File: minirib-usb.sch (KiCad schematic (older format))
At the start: 21 parts

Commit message: added test connector
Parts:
- added J?: Test_header, symbol Connector:Conn_01x06_Male
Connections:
- wire segments 65 -> 67
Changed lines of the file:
@@
 Wire Wire Line
 	5900 4750 5800 4750
+$Comp
+L Connector:Conn_01x06_Male J?
+U 1 1 610DD5AA
+P 8000 3000
+F 0 "J?" H 8200 3450 50  0000 C CNN
+F 1 "Test_header" H 8200 3350 50  0000 C CNN
+F 2 "" H 8000 3000 50  0001 C CNN
+F 3 "~" H 8000 3000 50  0001 C CNN
+	1    8000 3000
+	1    0    0    -1
+$EndComp
+$Comp
+L power:GND #PWR?
+U 1 1 610E094D
+P 8600 2850
+F 0 "#PWR?" H 8600 2600 50  0001 C CNN
+F 1 "GND" H 8605 2677 50  0001 C CNN
+F 2 "" H 8600 2850 50  0001 C CNN
+F 3 "" H 8600 2850 50  0001 C CNN
+	1    8600 2850
+	1    0    0    -1
+$EndComp
+Wire Wire Line
+	8200 2800 8600 2800
+Wire Wire Line
+	8600 2800 8600 2850
+Text GLabel 8200 2900 2    50   Input ~ 0
+~BUSY
+Text GLabel 8200 3000 2    50   Input ~ 0
+BUSY
+Text GLabel 8200 3100 2    50   Input ~ 0
+BUS-
+Text GLabel 8200 3200 2    50   Input ~ 0
+BUS+
+Text GLabel 8200 3300 2    50   Input ~ 0
+BIAS
 $EndSCHEMATC

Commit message: schematic rework
more closely following the original RIB schematic
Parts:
- removed Q?: 2N3906, symbol Device:Q_PNP_BCE
- removed Q? (x2): 2N3904, symbol Device:Q_NPN_BCE
- removed R? (x5): 4k7, symbol Device:R_Small
- removed U?: CA3140, symbol Amplifier_Operational:CA3140
- added C? (x5): 220pF, symbol Device:C_Small
- added D? (x4): D_TVS, symbol Device:D_TVS
- added D?: TXLED, symbol Device:LED_Small
- added D?: RXLED, symbol Device:LED_Small
- added Q? (x2): 2N3906, Package_TO_SOT_THT:TO-92_Inline, symbol Transistor_BJT:2N3906
- added Q? (x5): 2N3904, Package_TO_SOT_THT:TO-92_Inline, symbol Transistor_BJT:2N3904
- added R? (x8): 4k7, symbol Device:R_Small
- added R? (x2): 2k2, symbol Device:R_Small
- added R?: 20k, symbol Device:R_Small
- added R?: 3k, symbol Device:R_Small
- added R? (x3): 1k5, symbol Device:R_Small
- added U?: LM311, symbol Comparator:LM311
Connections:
- net labels added: ~CTS, ~DTR
- wire segments 67 -> 118
- no-connect marks 7 -> 8
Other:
- moved on the sheet: C?, J?, R?, U?

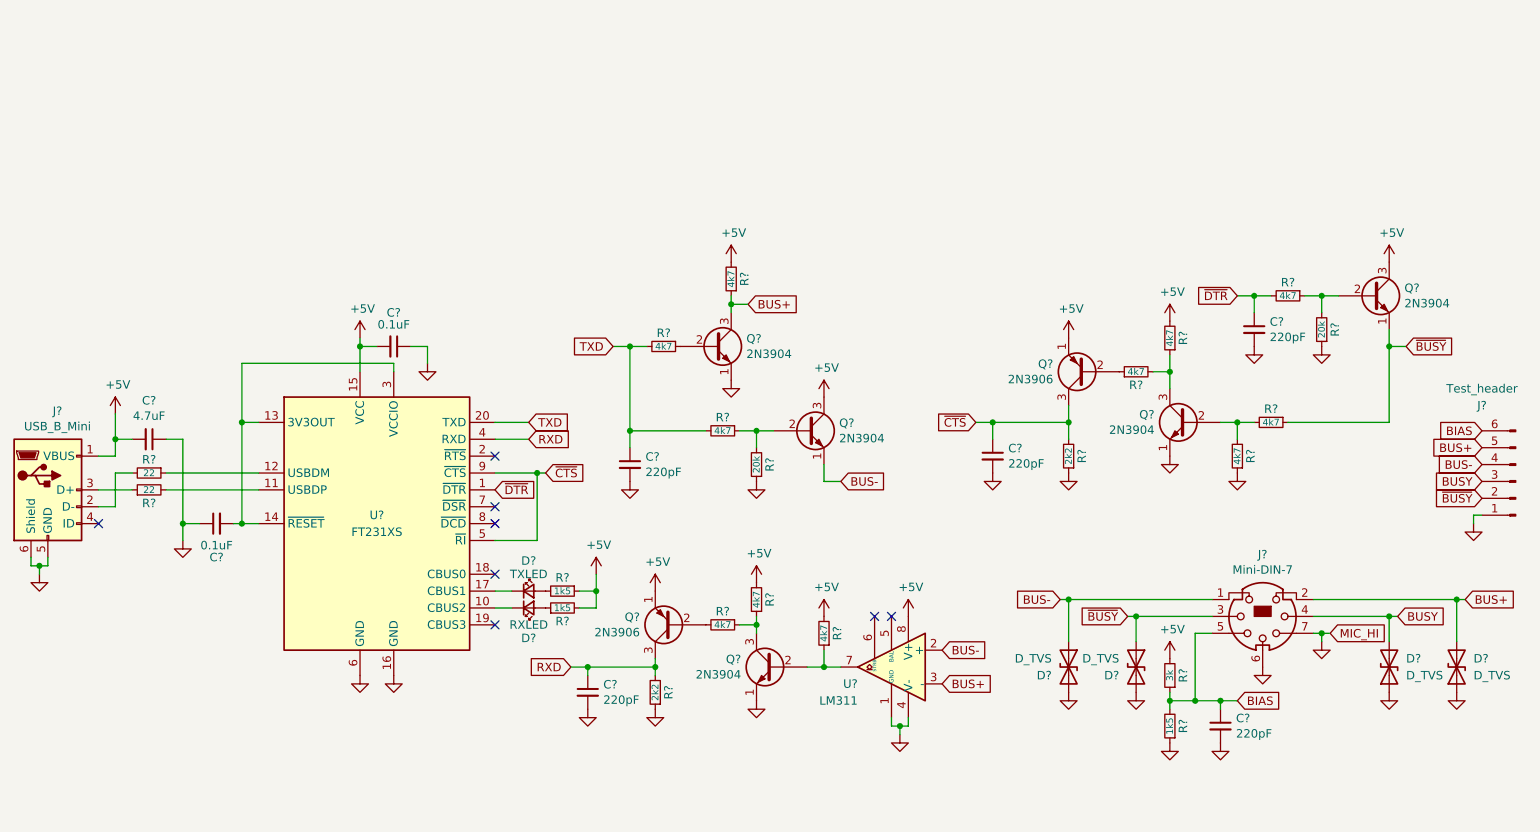
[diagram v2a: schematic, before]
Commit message: updated schematic with test headers and cleaned up
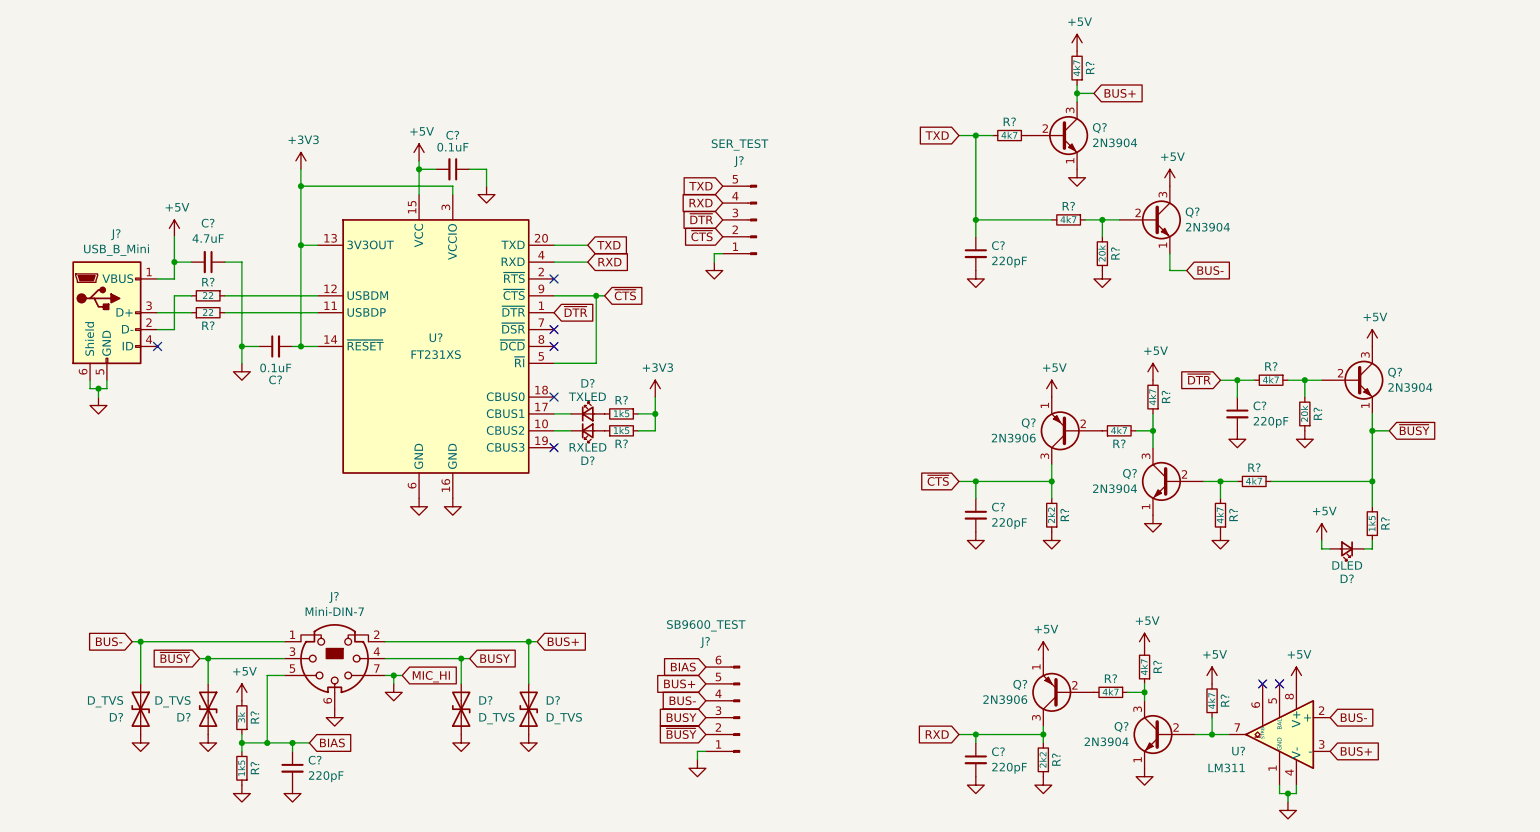
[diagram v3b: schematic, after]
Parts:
- added D?: DLED, symbol Device:LED_Small
- added J?: SER_TEST, symbol Connector:Conn_01x05_Male
- added R?: 1k5, symbol Device:R_Small
- J?: value Test_header -> SB9600_TEST
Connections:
- net +5V: now also D?.2 (A); no longer R?.1, R?.2
- net GND: now also J?.1 (Pin_1)
- net RXD: now also J?.4 (Pin_4)
- net TXD: now also J?.5 (Pin_5)
- net ~BUSY: now also R?.2
- net ~CTS: now also J?.2 (Pin_2)
- net ~DTR: now also J?.3 (Pin_3)
- net +3V3: now reaches C?.2, U?.13 (3V3OUT), U?.14 (~RESET), U?.3 (VCCIO)
- net +3V3: now also R?.1, R?.2
- new net: D?.1 (K), R?.1
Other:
- moved on the sheet: C?, D?, J?, Q?, R?, U?

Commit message: finalized initial schematic work
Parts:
- removed J?: Mini-DIN-7, symbol Connector:Mini-DIN-7
- added J2: Mini-DIN-6-Shielded, MiniRIB-USB:MDJ-006-FS, symbol MiniDin:Mini-DIN-6-Shielded
- C1, C2, C3, C4, C5, C6, C7, C8: renamed from C?; footprint (none) -> Capacitor_SMD:C_0805_2012Metric_Pad1.18x1.45mm_HandSolder
- D1, D2, D3, D4, D5, D6, D7: renamed from D?; footprint (none) -> Diode_SMD:D_1206_3216Metric_Pad1.42x1.75mm_HandSolder
- J1: renamed from J?; footprint (none) -> Connector_USB:USB_Mini-B_Wuerth_65100516121_Horizontal
- J3: renamed from J?; footprint (none) -> Connector_PinHeader_1.27mm:PinHeader_1x06_P1.27mm_Vertical
- J4: renamed from J?; footprint (none) -> Connector_PinHeader_1.27mm:PinHeader_1x05_P1.27mm_Vertical
- R1, R10, R11, R12, R13, R14, R15, R16, R17, R18, R19, R2, R20, R21, R22, R3, R4, R5, R6, R7, R8, R9: renamed from R?; footprint (none) -> Resistor_SMD:R_0805_2012Metric_Pad1.20x1.40mm_HandSolder
- U2: renamed from U?; footprint (none) -> Package_SO:SOIC-8_3.9x4.9mm_P1.27mm
- gave numbers to parts that had none: 8
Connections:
- net BIAS: now also J2.2
- net BUS+: now also J2.5
- net BUS-: now also J2.6
- net BUSY: now also J2.3
- net GND: now also J2.1, J2.SH
- net ~BUSY: now also J2.4

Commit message: more work on schematic and PCB
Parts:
- removed J3: SB9600_TEST, Connector_PinHeader_1.27mm:PinHeader_1x06_P1.27mm_Vertical, symbol Connector:Conn_01x06_Male
- removed J4: SER_TEST, Connector_PinHeader_1.27mm:PinHeader_1x05_P1.27mm_Vertical, symbol Connector:Conn_01x05_Male
- removed Q1, Q4, Q5, Q6, Q7: 2N3904, Package_TO_SOT_THT:TO-92_Inline, symbol Transistor_BJT:2N3904
- removed Q2, Q3: 2N3906, Package_TO_SOT_THT:TO-92_Inline, symbol Transistor_BJT:2N3906
- removed U2: LM311, Package_SO:SOIC-8_3.9x4.9mm_P1.27mm, symbol Comparator:LM311
- added Q1, Q4, Q5, Q6, Q7: MMST3904-7-F, Package_TO_SOT_SMD:SOT-323_SC-70_Handsoldering, symbol Device:Q_NPN_BEC
- added Q2, Q3: MMST3906-7-F, Package_TO_SOT_SMD:SOT-323_SC-70_Handsoldering, symbol Device:Q_PNP_BEC
- added U2: TL081H, Package_TO_SOT_SMD:SOT-23-5_HandSoldering, symbol MiniDin:TL081H
- D1, D2, D3, D4, D5, D6, D7: footprint Diode_SMD:D_1206_3216Metric_Pad1.42x1.75mm_HandSolder -> Diode_SMD:D_0805_2012Metric_Pad1.15x1.40mm_HandSolder
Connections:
- net +5V: now also Q2.2 (E), Q3.2 (E), Q4.3 (C), Q7.3 (C), U2.5 (V+); no longer D7.2 (A), R17.2
- net BUS+: now also Q1.3 (C), U2.4 (-)
- net BUS-: now also Q4.2 (E), U2.3 (+)
- net BUSY: now also R14.2, R16.1, R22.1, Q6.3 (C)
- net GND: now also D7.1 (K), Q1.2 (E), Q5.2 (E), Q6.2 (E), U2.2 (V-)
- net RXD: now also Q2.3 (C)
- net ~BUSY: now also Q7.2 (E); no longer R22.2
- net ~CTS: now also Q3.3 (C)
- net at R7.1: now also Q1.1 (B)
- net at R10.1, R12.2: now also Q4.1 (B)
- net at R17.1: now also Q5.1 (B)
- net at R13.1, R15.1: now also Q5.3 (C)
- net at R13.2: now also Q2.1 (B)
- net at R20.1, R21.2: now also Q7.1 (B)
- net at R18.2, R19.2: now also Q6.1 (B)
- net at R14.1: now also Q3.1 (B)
- new net: R17.2, U2.1
- new net: D7.2 (A), R22.2
- no-connect marks 8 -> 6
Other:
- moved on the sheet: D7, R17, R22

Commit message: Finalized rev A schematic and PCB
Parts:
- removed J1: USB_B_Mini, Connector_USB:USB_Mini-B_Wuerth_65100516121_Horizontal, symbol Connector:USB_B_Mini
- added J1: USB_B_Micro, Connector_USB:USB_Micro-B_Wuerth_629105150521, symbol Connector:USB_B_Micro
- J2: footprint MiniRIB-USB:MDJ-006-FS -> MiniRIB-USB:KMDGX-6S-BS
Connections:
- net +5V: now also J1.1 (VBUS)
- net GND: now also J1.5 (GND), J1.6 (Shield)
- net at R1.2: now also J1.2 (D-)
- net at R2.1: now also J1.3 (D+)
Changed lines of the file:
@@
-$EndComp
-$Comp
-L Connector:USB_B_Mini J1
-U 1 1 60FEF9B3
-P 1650 2800
-F 0 "J1" H 1707 3267 50  0000 C CNN
-F 1 "USB_B_Mini" H 1707 3176 50  0000 C CNN
-F 2 "Connector_USB:USB_Mini-B_Wuerth_65100516121_Horizontal" H 1800 2750 50  0001 C CNN
-F 3 "~" H 1800 2750 50  0001 C CNN
-	1    1650 2800
-	1    0    0    -1
 $EndComp
 $Comp
@@
 F 0 "J2" H 3000 5217 50  0000 C CNN
 F 1 "Mini-DIN-6-Shielded" H 3000 5126 50  0000 C CNN
-F 2 "MiniRIB-USB:MDJ-006-FS" H 3000 4850 50  0001 C CNN
+F 2 "MiniRIB-USB:KMDGX-6S-BS" H 3000 4850 50  0001 C CNN
 F 3 "http://service.powerdynamics.com/ec/Catalog17/Section%2011.pdf" H 3000 4850 50  0001 C CNN
 	1    3000 4850
@@
 	-1   0    0    -1
 $EndComp
+$Comp
+L Connector:USB_B_Micro J1
+U 1 1 61BB19CD
+P 1650 2800
+F 0 "J1" H 1707 3267 50  0000 C CNN
+F 1 "USB_B_Micro" H 1707 3176 50  0000 C CNN
+F 2 "Connector_USB:USB_Micro-B_Wuerth_629105150521" H 1800 2750 50  0001 C CNN
+F 3 "~" H 1800 2750 50  0001 C CNN
+	1    1650 2800
+	1    0    0    -1
+$EndComp
 $EndSCHEMATC
